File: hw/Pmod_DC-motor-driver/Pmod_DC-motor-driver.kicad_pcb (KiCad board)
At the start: 2 copper layers, 37.7 x 16.9 mm, 16 parts, among them J1 Encoder, J6 Encoder, J8 Conn_02x06_Odd_Even, U6 DRV8833

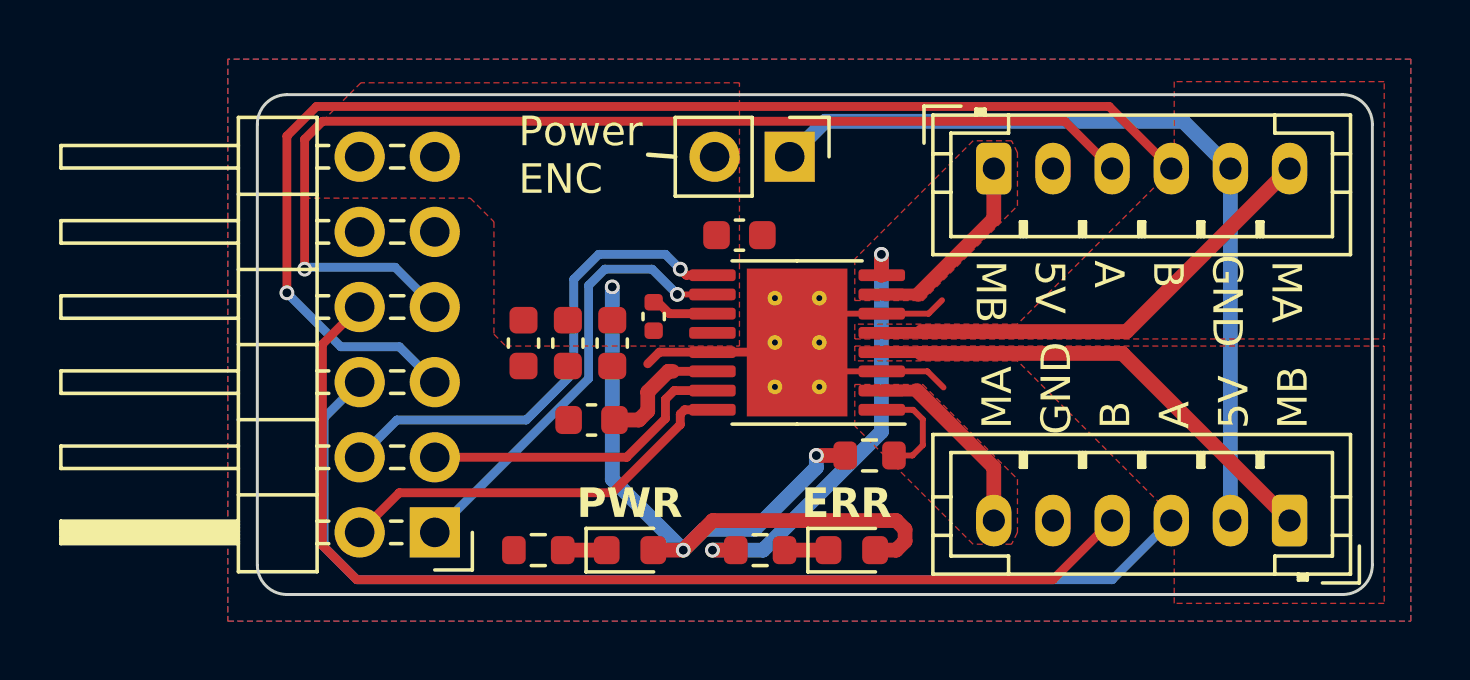
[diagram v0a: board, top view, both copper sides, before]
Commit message: Add divider to ENC line
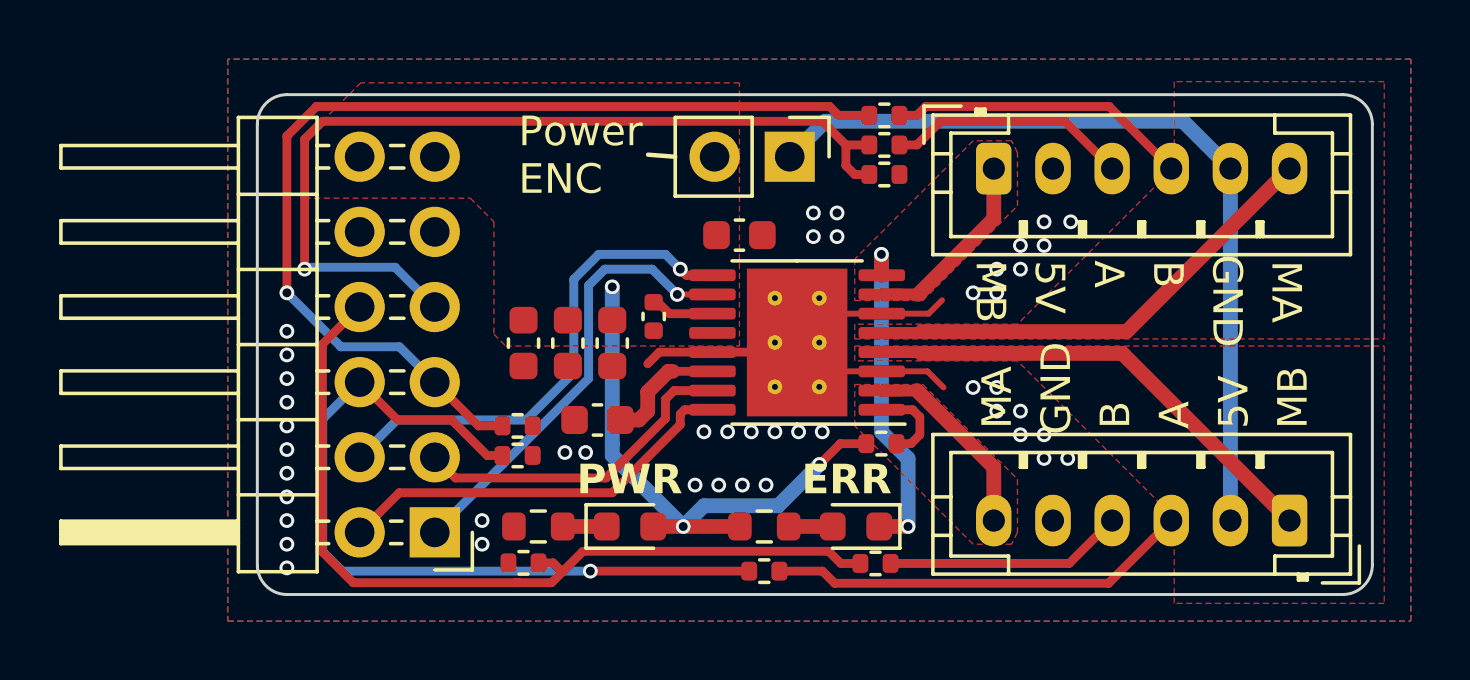
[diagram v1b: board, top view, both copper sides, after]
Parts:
- added R10: 10k, Resistor_SMD:R_0402_1005Metric, F.Cu at (143.0, 91.0)
- added R3: 10k, Resistor_SMD:R_0402_1005Metric, F.Cu at (155.2, 77.9)
- added R4: 4k7, Resistor_SMD:R_0402_1005Metric, F.Cu at (155.2, 76.9)
- added R5: 4k7, Resistor_SMD:R_0402_1005Metric, F.Cu at (155.2, 75.9)
- added R6: 4k7, Resistor_SMD:R_0402_1005Metric, F.Cu at (151.1, 91.3)
- added R7: 4k7, Resistor_SMD:R_0402_1005Metric, F.Cu at (154.9, 91.0)
- added R8: 10k, Resistor_SMD:R_0402_1005Metric, F.Cu at (142.8, 86.4)
- added R9: 10k, Resistor_SMD:R_0402_1005Metric, F.Cu at (142.8, 87.4)
- R24: footprint Resistor_SMD:R_0603_1608Metric -> Resistor_SMD:R_0402_1005Metric
- moved D1 0.81 mm to (154.2, 89.8), turned to 180 degrees
- moved R1 0.81 mm to (151.1, 89.8), turned to 0 degrees
- moved D2 0.80 mm to (146.6, 89.8)
- moved R2 0.80 mm to (143.5, 89.8)
- moved R24 0.57 mm to (155.1, 87.0)
- moved C15 0.20 mm to (145.5, 86.2)
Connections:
- D1 pad 2: +5V -> Net-(D1-A)
- J1 pad 3: /ENC_B2 -> Net-(J1-Pin_3)
- J1 pad 4: /ENC_A2 -> Net-(J1-Pin_4)
- J6 pad 3: /ENC_A1 -> Net-(J6-Pin_3)
- J6 pad 4: /ENC_B1 -> Net-(J6-Pin_4)
- R1 pad 1: Net-(D1-K) -> +5V
- R1 pad 2: Net-(U6-nFAULT) -> Net-(D1-A)
- U6 pad 8: Net-(U6-nFAULT) -> Net-(D1-K)
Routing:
- net Net-(U6-nFAULT): track 14.9 -> 0.00 mm, vias 2 -> 0
- net Net-(J6-Pin_3): track 0.00 -> 14.3 mm
- net Net-(J1-Pin_4): track 0.00 -> 10.2 mm
- net Net-(D1-K): track 1.49 -> 11.3 mm, vias 0 -> 2
- net /ENC_A1: track 36.0 -> 26.8 mm, vias 0 -> 1
- net Net-(J1-Pin_3): track 0.00 -> 8.18 mm
- net +5V: track 27.5 -> 19.4 mm
- net Net-(J6-Pin_4): track 0.00 -> 8.09 mm
- net /ENC_A2: track 42.7 -> 34.7 mm
- net /ENC_B1: track 36.6 -> 29.1 mm
- net /ENC_B2: track 37.6 -> 30.7 mm
- net Net-(D1-A): track 0.00 -> 1.49 mm
- net Net-(U6-nSLEEP): track 3.51 -> 2.90 mm
- net /PWM-B2: track 10.7 -> 11.3 mm
- net GND: vias 0 -> 45
